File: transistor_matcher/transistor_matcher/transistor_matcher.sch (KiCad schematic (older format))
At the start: 17 parts

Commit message: updated schematic for VBE measurement, started on board layout
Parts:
- removed J?: USB_B_Mini, symbol Connector:USB_B_Mini
- removed SW?: SW_MODE_DPDT, symbol Switch:SW_Push_DPDT
- added D1, D2: 1N4448, sparkfun/SparkFun-KiCad-Libraries/Footprints/Silicon-Custom.pretty:DIODE-1N4001, symbol transistor_matcher:1N4448
- added J1: USB_B_Micro, digikey/digikey-kicad-library/digikey-footprints.pretty:USB_Micro_AB_Female_0475890001, symbol transistor_matcher:USB_B_Micro
- added R2: 22K, 4ms/4ms-kicad-lib/4ms-footprints.pretty:Resistor_TH_300, symbol Device:R
- added SW1, SW2: SW_DPDT_x2, KiCad/kicad-footprints/Button_Switch_THT.pretty:SW_E-Switch_EG1271_DPDT, symbol Switch:SW_DPDT_x2
- J2: renamed from J?; footprint (none) -> 4ms/4ms-kicad-lib/lib-footprints/4ms_Connector.pretty:Pins_2x03_2.54mm_TH_ISP
- J3: renamed from J?; footprint (none) -> sparkfun/SparkFun-KiCad-Libraries/Footprints/Connectors.pretty:JST-4-PTH
- JP1, JP2: renamed from JP?; footprint (none) -> keebio/Keebio-Parts.pretty:solder_jumper
- Q1, Q2: renamed from Q?; footprint Package_TO_SOT_THT:TO-92_Inline -> transistor_matcher:BJT_Slot
- R1: renamed from R?; value 1K -> 22K; footprint (none) -> 4ms/4ms-kicad-lib/4ms-footprints.pretty:Resistor_TH_300
- R3: renamed from R?; value 2K2 -> 100; footprint (none) -> 4ms/4ms-kicad-lib/4ms-footprints.pretty:Resistor_TH_300
- R4, R5: renamed from R?; value 1K -> 100K; footprint (none) -> 4ms/4ms-kicad-lib/4ms-footprints.pretty:Resistor_TH_300
- R6, R7: renamed from R?; footprint (none) -> 4ms/4ms-kicad-lib/4ms-footprints.pretty:Resistor_TH_300
- RV1: renamed from RV?; value 2K TRIM -> 10K TRIM; footprint (none) -> KiCad/Potentiometers.pretty:Potentiometer_Trimmer_Bourns_PV36W
- U1: renamed from U?; footprint Package_SO:SOIC-8_3.9x4.9mm_P1.27mm -> 4ms/4ms-kicad-lib/4ms-footprints.pretty:SOIC-8_3.9x4.9mm_Pitch1.27mm
- U2: renamed from U?; footprint Package_DIP:DIP-8_W7.62mm -> KiCad/Housings_DIP.pretty:DIP-8_W7.62mm_Socket
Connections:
- net labels removed: VC, VE
- wire segments 92 -> 100
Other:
- note added: "-VS + .01V < 0.6V + VCM +/- abs(VDIFF)*G / 10 < +VS - .1V\n.01V < 0.6 + 0.6 + 5 / 10 = 1.7V < 4.9V"
- note added: "By setting the base voltage to 2.5V,\nwe ensure the measurement point is\neither 3.1V or 1.9V, depending on\nPNP or NPN. This is to keep the CMRR\nIn the tolerences specified in the datasheet.\nThe diode ensures the resistors are always on\nand sets VC to be about 600mV the other way"
- note added: "Ideal VBE diff < 50uV\nTherefore Gain must be 500-1000\n80K / (G-5)\n100 => G=805 => 6mV resolution"
- note removed: "By setting the base voltage to 2.5V,\nwe ensure the measurement point is\neither 3.1V or 1.9V, depending on\nPNP or NPN. This is to keep the CMRR\nIn the tolerences specified in the datasheet.\nThe resistor values set the current so that\nthe voltage at the emitter is about 600mV\nthe other way, so that the circuit is symetrical\nand can be used for both PNP and NPN with\nthe same currents"
- note removed: "Gain TBD, but suspect about 50\n80K / (G-5)"
- moved on the sheet: Q1, Q2, R1, R3, R4, R5, RV1, U1

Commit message: simplfied based on emperical tests
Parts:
- removed D1, D2: 1N4448, sparkfun/SparkFun-KiCad-Libraries/Footprints/Silicon-Custom.pretty:DIODE-1N4001, symbol transistor_matcher:1N4448
- removed J1: USB_B_Micro, digikey/digikey-kicad-library/digikey-footprints.pretty:USB_Micro_AB_Female_0475890001, symbol transistor_matcher:USB_B_Micro
- removed J2: USBasp CONN, 4ms/4ms-kicad-lib/lib-footprints/4ms_Connector.pretty:Pins_2x03_2.54mm_TH_ISP, symbol Connector_Generic:Conn_02x03_Counter_Clockwise
- removed JP1, JP2: Jumper, keebio/Keebio-Parts.pretty:solder_jumper, symbol Device:Jumper
- removed R2: 22K, 4ms/4ms-kicad-lib/4ms-footprints.pretty:Resistor_TH_300, symbol Device:R
- removed U2: ATtiny85-20PU, KiCad/Housings_DIP.pretty:DIP-8_W7.62mm_Socket, symbol MCU_Microchip_ATtiny:ATtiny85-20PU
- added U2: LM317_3PinPackage, KiCad/TO_SOT_Packages_THT.pretty:TO-220-3_Horizontal, symbol Regulator_Linear:LM317_3PinPackage
- added U3: Teensy2.0_(Arduino), teensy:Teensy2.0, symbol teensy:Teensy2.0_(Arduino)
- J3: footprint sparkfun/SparkFun-KiCad-Libraries/Footprints/Connectors.pretty:JST-4-PTH -> sparkfun/SparkFun-KiCad-Libraries/Footprints/Connectors.pretty:JST-4-PTH-VERT
- R1: value 22K -> 10K; footprint 4ms/4ms-kicad-lib/4ms-footprints.pretty:Resistor_TH_300 -> KiCad/Resistors_ThroughHole.pretty:R_Axial_DIN0204_L3.6mm_D1.6mm_P1.90mm_Vertical
- R3, R6, R7: footprint 4ms/4ms-kicad-lib/4ms-footprints.pretty:Resistor_TH_300 -> KiCad/Resistors_ThroughHole.pretty:R_Axial_DIN0204_L3.6mm_D1.6mm_P1.90mm_Vertical
- R4, R5: value 100K -> 220; footprint 4ms/4ms-kicad-lib/4ms-footprints.pretty:Resistor_TH_300 -> KiCad/Resistors_ThroughHole.pretty:R_Axial_DIN0204_L3.6mm_D1.6mm_P1.90mm_Vertical
- RV1: value 10K TRIM -> 50K TRIM
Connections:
- net labels removed: MISO, MOSI, RST, SCK, VCC
- wire segments 100 -> 77
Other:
- note added: "By setting the base voltage to 2.5V,\nwe ensure the measurement point is\neither 3.1V or 1.9V, depending on\nPNP or NPN. This is to keep the CMRR\nIn the tolerences specified in the datasheet:\n\n-VS + .01V < 0.6V + VCM +/- abs(VDIFF)*G / 10 < +VS - .1V\n.01V < 0.6 + 0.6 + 5 / 10 = 1.7V < 4.9V"
- note added: "Literature suggests very good matching is <50uV\nfor 2N390X, I’ve seen 3-9mV variance\nRg = 80K / (G-5)\n100 => G=805 => 6uV resolution\n1K => G=85 => 57uV resolution\nG = 5 => 1mV resolution"
- note added: "TODO: display may have pull-ups"
- note removed: "-VS + .01V < 0.6V + VCM +/- abs(VDIFF)*G / 10 < +VS - .1V\n.01V < 0.6 + 0.6 + 5 / 10 = 1.7V < 4.9V"
- note removed: "By setting the base voltage to 2.5V,\nwe ensure the measurement point is\neither 3.1V or 1.9V, depending on\nPNP or NPN. This is to keep the CMRR\nIn the tolerences specified in the datasheet.\nThe diode ensures the resistors are always on\nand sets VC to be about 600mV the other way"
- note removed: "Ideal VBE diff < 50uV\nTherefore Gain must be 500-1000\n80K / (G-5)\n100 => G=805 => 6mV resolution"
- note removed: "TODO: it says in the datasheet not to do this,\nto use a low-impedence voltage source like\nan op-amp instead, that it’s bad for performance.\nTry without and see if it’s okay"
- note removed: "With WIRE lib, SDA=PORTB0 (5), SCL=PORTB2 (7)"
- note removed: "remove jumpers to disconnect the pullups when programming"
- note removed: "the displays ordered are I2C, which the ATTINY85\ndoesn’t support natively. However, there seems to\nbe a solid bit-banged implementation online which\nwill hopefully work. Otherwise we’ll have to use a\nbigger chip, maybe a Teensy"
- moved on the sheet: J3, Q1, Q2, R1, R3, R4, R5, R6, R7, RV1, SW1A, SW1B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

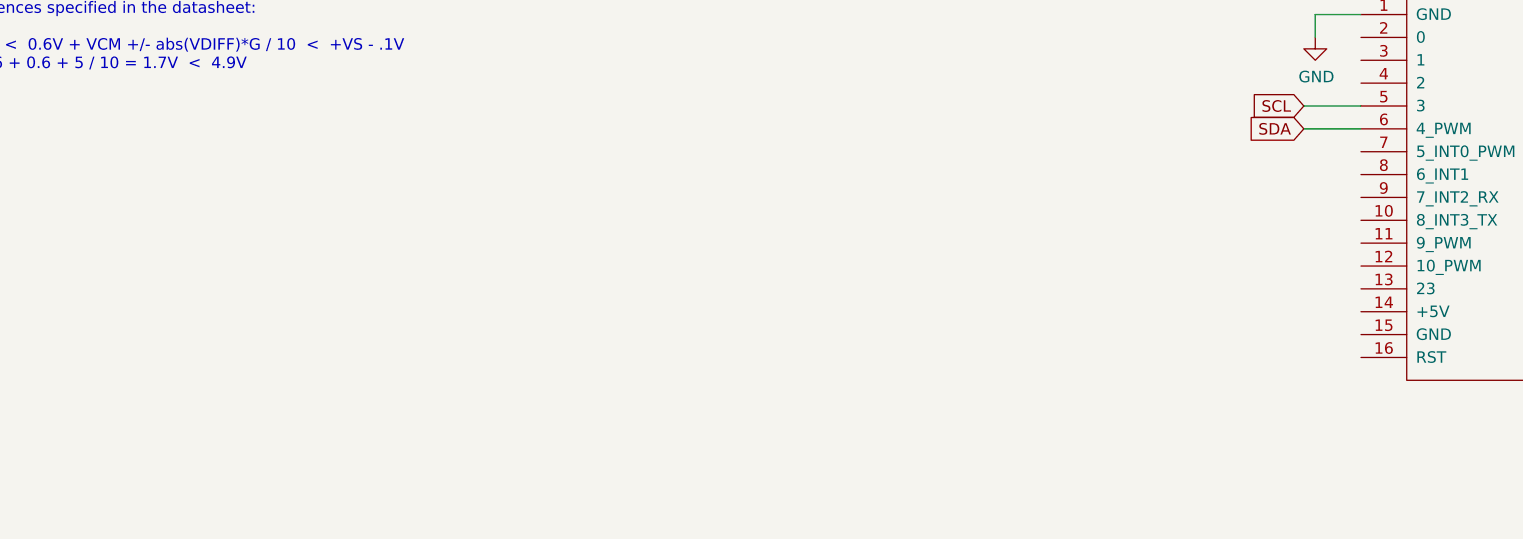
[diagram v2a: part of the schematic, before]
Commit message: basic sketch to prove inst. amp is working I think we really need a constant upper reference voltage
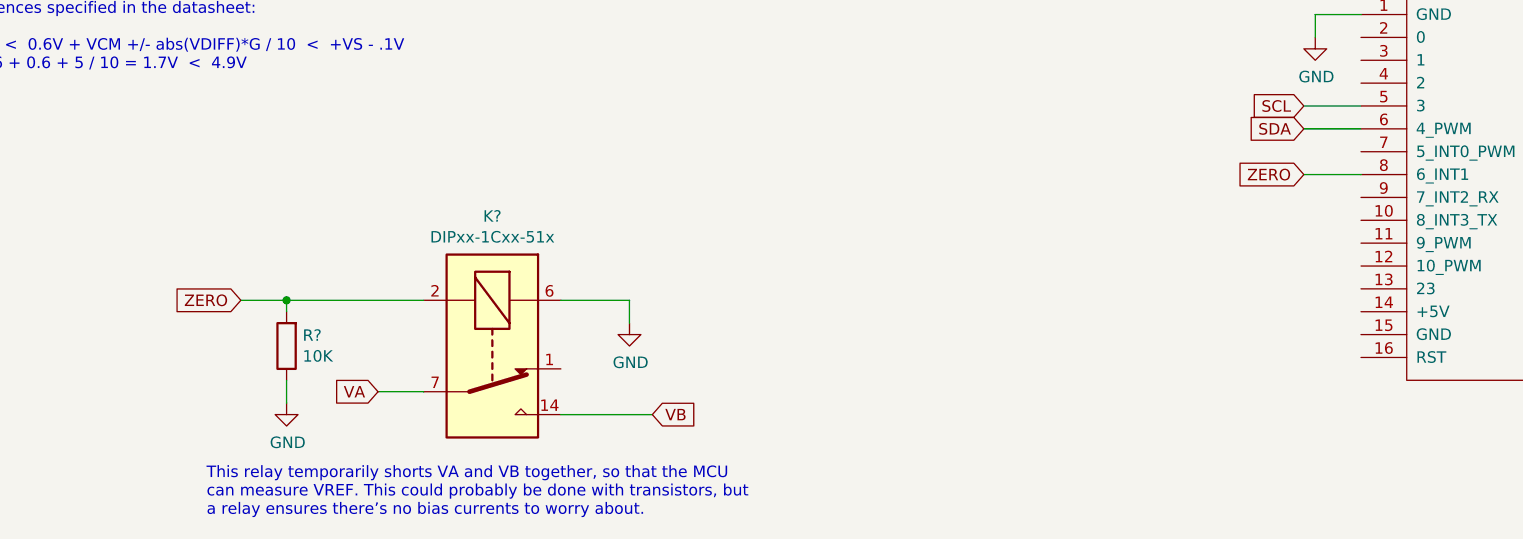
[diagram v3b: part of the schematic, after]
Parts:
- added K?: DIPxx-1Cxx-51x, Relay_THT:Relay_StandexMeder_DIP_LowProfile, symbol Relay:DIPxx-1Cxx-51x
- added R?: 10K, KiCad/Resistors_ThroughHole.pretty:R_Axial_DIN0204_L3.6mm_D1.6mm_P1.90mm_Vertical, symbol Device:R
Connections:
- net GND: now also K?.6, R?.1
- net VA: now also K?.7, K?.8
- net VB: now also K?.14
- net ZERO: now reaches U3.8 (6_INT1)
- net ZERO: now also K?.2, R?.2
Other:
- note added: "This relay temporarily shorts VA and VB together, so that the MCU\ncan measure VREF. This could probably be done with transistors, but\na relay ensures there’s no bias currents to worry about."
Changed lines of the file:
@@
 Wire Wire Line
 	10800 4700 10350 4700
+$Comp
+L Relay:DIPxx-1Cxx-51x K?
+U 1 1 5E7FFE7E
+P 5150 6050
+F 0 "K?" V 4583 6050 50  0000 C CNN
+F 1 "DIPxx-1Cxx-51x" V 4674 6050 50  0000 C CNN
+F 2 "Relay_THT:Relay_StandexMeder_DIP_LowProfile" H 5600 6000 50  0001 L CNN
+F 3 "https://standexelectronics.com/wp-content/uploads/datasheet_reed_relay_DIP.pdf" H 5150 6050 50  0001 C CNN
+	1    5150 6050
+	0    1    1    0
+$EndComp
+Text GLabel 4650 6250 0    50   Input ~ 0
+VA
+Wire Wire Line
+	4650 6250 4850 6250
+Text GLabel 5850 6350 2    50   Input ~ 0
+VB
+Wire Wire Line
+	5850 6350 5450 6350
+$Comp
+L power:GND #PWR?
+U 1 1 5E80C2C5
+P 5750 5950
+F 0 "#PWR?" H 5750 5700 50  0001 C CNN
+F 1 "GND" H 5755 5777 50  0000 C CNN
+F 2 "" H 5750 5950 50  0001 C CNN
+F 3 "" H 5750 5950 50  0001 C CNN
+	1    5750 5950
+	1    0    0    -1
+$EndComp
+Wire Wire Line
+	5750 5950 5750 5850
+Wire Wire Line
+	5750 5850 5450 5850
+$Comp
+L Device:R R?
+U 1 1 5E80EAE7
+P 4250 6050
+F 0 "R?" H 4180 6004 50  0000 R CNN
+F 1 "10K" H 4180 6095 50  0000 R CNN
+F 2 "KiCad/Resistors_ThroughHole.pretty:R_Axial_DIN0204_L3.6mm_D1.6mm_P1.90mm_Vertical" V 4180 6050 50  0001 C CNN
+F 3 "~" H 4250 6050 50  0001 C CNN
+	1    4250 6050
+	-1   0    0    1
+$EndComp
+Wire Wire Line
+	4250 5900 4250 5850
+Wire Wire Line
+	4250 5850 4850 5850
+Text GLabel 4050 5850 0    50   Input ~ 0
+ZERO
+Wire Wire Line
+	4050 5850 4250 5850
+Connection ~ 4250 5850
+Text GLabel 8700 5300 0    50   Input ~ 0
+ZERO
+Wire Wire Line
+	8700 5300 8950 5300
+Text Notes 3900 6800 0    50   ~ 0
+This relay temporarily shorts VA and VB together, so that the MCU\ncan measure VREF. This could probably be done with transistors, but\na relay ensures there’s no bias currents to worry about.
+$Comp
+L power:GND #PWR?
+U 1 1 5E81680B
+P 4250 6300
+F 0 "#PWR?" H 4250 6050 50  0001 C CNN
+F 1 "GND" H 4255 6127 50  0000 C CNN
+F 2 "" H 4250 6300 50  0001 C CNN
+F 3 "" H 4250 6300 50  0001 C CNN
+	1    4250 6300
+	1    0    0    -1
+$EndComp
+Wire Wire Line
+	4250 6300 4250 6200
 $EndSCHEMATC
